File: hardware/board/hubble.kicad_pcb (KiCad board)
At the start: 2 copper layers, 100 x 100 mm, 118 parts, among them J1 POWER, J2 SWD, J3 USB_B_Receptacle, J4 EXT, J5 Left, J6 Right, J7 Bottom, J8 EXT, J9 EXT, SW1 POWER, SW2 Reset, U1 LD1117-3.3, U10 OPA4197, U11 MCP6004, U2 LM4040-10, U3 LM4040-10, U4 MUX509, U5 ATSAMD51J20A-M, U6 AD5685R?RUZ, U7 MUX509, U8 MUX509, U9 MUX509, Y1 32.768 kHz

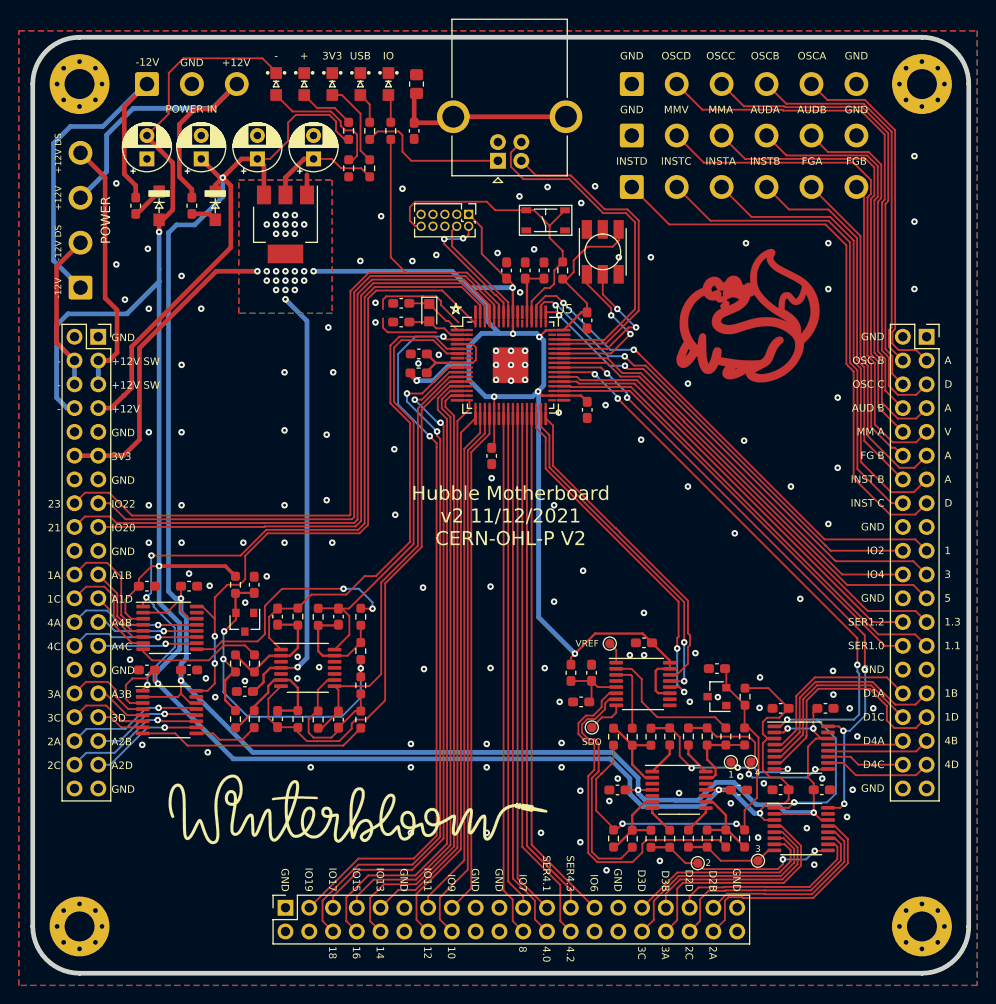
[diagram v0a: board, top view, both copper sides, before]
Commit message: More updates to the board design
- Added polyfuses for downstream power
- Added breakout header for external, panel-mounted USB port
- Added I/O breakout for the switches and buttons on the front control panel
- Made the MCU footprint a hybrid QFP/QFN footprint
- Add a nice illustration to the board backside
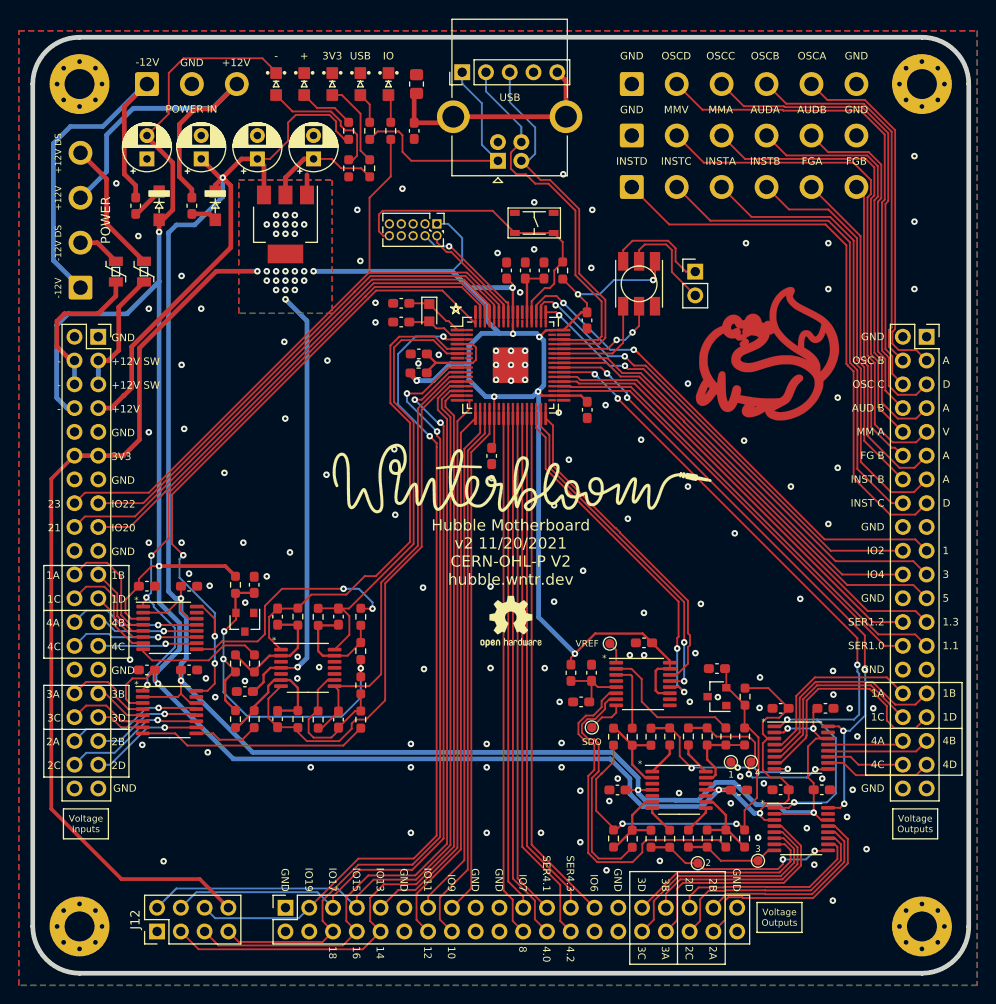
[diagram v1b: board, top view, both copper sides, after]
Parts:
- added F1: 1A Polyfuse, winterbloom:Littelfuse_0805L, F.Cu at (86.9, 74.0)
- added F2: 1A Polyfuse, winterbloom:Littelfuse_0805L, F.Cu at (83.9, 74.0)
- added G***: LOGO, hubble:hubble-illustration, B.Cu at (127.7, 97.6)
- added J10: Dotstars, Connector_PinHeader_2.54mm:PinHeader_1x02_P2.54mm_Vertical, F.Cu at (145.8, 74.0)
- added J11: USB, Connector_PinHeader_2.54mm:PinHeader_1x05_P2.54mm_Vertical, F.Cu at (120.9, 52.7)
- added J12: FRONT, Connector_PinHeader_2.54mm:PinHeader_2x04_P2.54mm_Vertical, F.Cu at (88.3, 144.5)
- added REF**: OSHW-Logo2_7.3x6mm_SilkScreen, Symbol:OSHW-Logo2_7.3x6mm_SilkScreen, F.Cu at (126.1, 111.4)
- J3: value USB_B_Receptacle -> USB B
- U6: value AD5685R?RUZ -> AD5689R?RUZ
- moved G*** 39.5 mm to (127.3, 96.1)
- moved D3 5.17 mm to (139.8, 75.3)
- moved ? 4.56 mm to (153.5, 82.7)
- moved J2 3.54 mm to (118.2, 68.9)
- moved SW2 1.25 mm to (128.6, 68.8), turned to 180 degrees
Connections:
- J7 pad 4: Net-(J7-Pad4) -> GND
- SW1 pad 2: -12VDOWNSTREAM -> Net-(F2-Pad1)
- SW1 pad 4: +12VDOWNSTREAM -> Net-(F1-Pad2)
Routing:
- net +3V3: track 253.5 -> 315.9 mm, vias 35 -> 37
- net /IO15: track 64.8 -> 87.8 mm
- net /IO14: track 66.0 -> 88.9 mm
- net /IO17: track 70.9 -> 88.6 mm
- net (no net): track 17.5 -> 0.00 mm
- net /IO16: track 69.1 -> 86.6 mm
- net /IO23: track 89.9 -> 74.2 mm
- net /IO22: track 71.1 -> 55.8 mm
- net /IO21: track 73.1 -> 58.4 mm
- net Net-(F1-Pad2): track 0.00 -> 14.4 mm
- net +12VDOWNSTREAM: track 27.9 -> 13.6 mm
- net /IO20: track 69.1 -> 55.0 mm
- net /IO18: track 75.8 -> 87.9 mm
- net /IO19: track 78.4 -> 90.5 mm
- net Net-(D3-Pad6): track 0.00 -> 11.5 mm
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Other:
- board text added: "*"
- board text added: "2B"
- board text added: "2D"
- board text added: "3B"
- board text added: "Hubble Motherboard v2 11/20/2021 CERN-OHL-P V2 hubble.wntr.dev"
- board text added: "Voltage Inputs"
- board text added: "Voltage Outputs"
- board text removed: "A1B"
- board text removed: "A1D"
- board text removed: "A2B"
- board text removed: "A2D"
- board text removed: "A3B"
- board text removed: "A4B"
- board text removed: "A4C"
- board text removed: "D1A"
- board text removed: "D1C"
- board text removed: "D2B"
- board text removed: "D2D"
- board text removed: "D3B"
- board text removed: "D3D"
- board text removed: "D4A"
- board text removed: "D4C"
- board text removed: "Hubble Motherboard v2 11/12/2021 CERN-OHL-P V2"
